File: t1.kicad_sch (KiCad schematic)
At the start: 47 parts, among them J1 Barrel_Jack_Switch, J2 USB_B, J3 P1, J4 2x2M, J5 ICSP1, J6 P2, U1 ATmega8U2-AU, Y1 16MHz

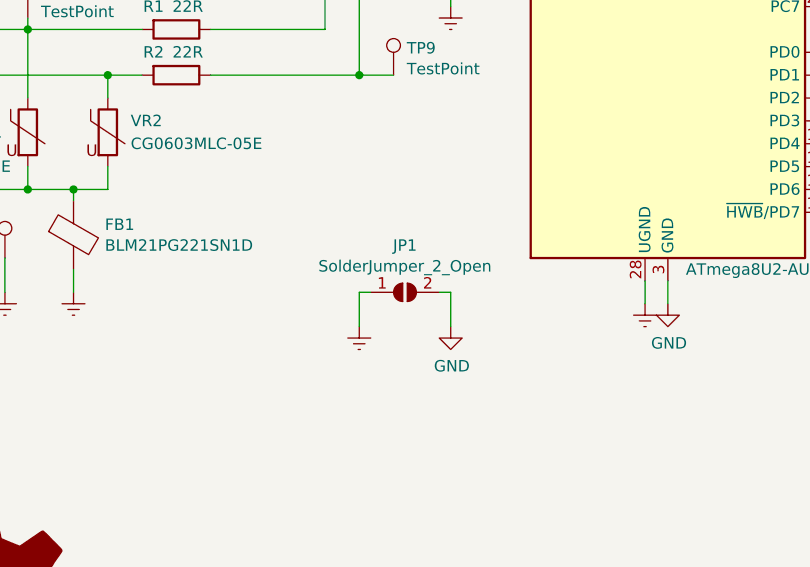
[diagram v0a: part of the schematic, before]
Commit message: Fixed ERC issues
- Connector names changed from Male to Pin (OMG!)
- Updated power components from KiCad 8 lib
- Synzed the PCB
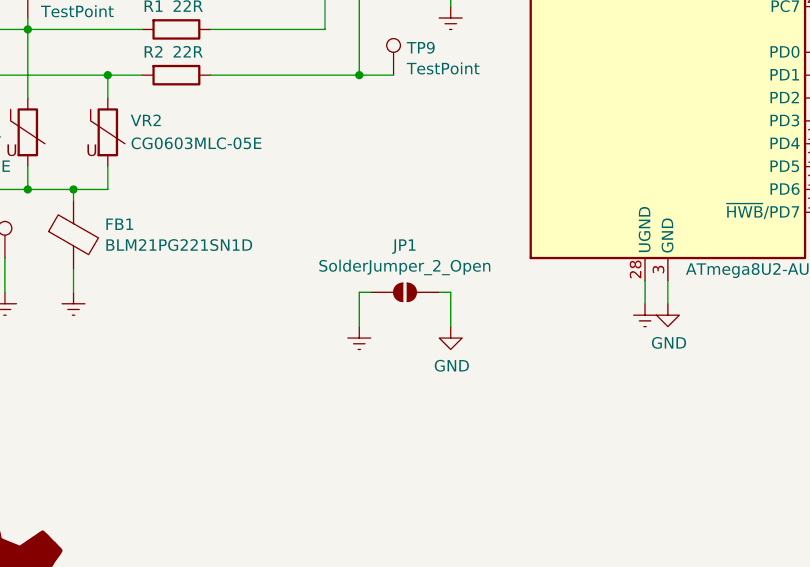
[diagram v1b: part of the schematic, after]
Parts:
- J3: symbol Connector:Conn_01x05_Male -> Connector:Conn_01x05_Pin
- J6: symbol Connector:Conn_01x06_Male -> Connector:Conn_01x06_Pin
